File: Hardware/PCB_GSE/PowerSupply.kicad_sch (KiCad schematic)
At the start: 64 parts, among them J8 Vin_XT30PW-F, U1 L6981N33DR, U3 MPQ9843GLE-5-AEC1-Z, U7 LM2673SX-12_NOPB

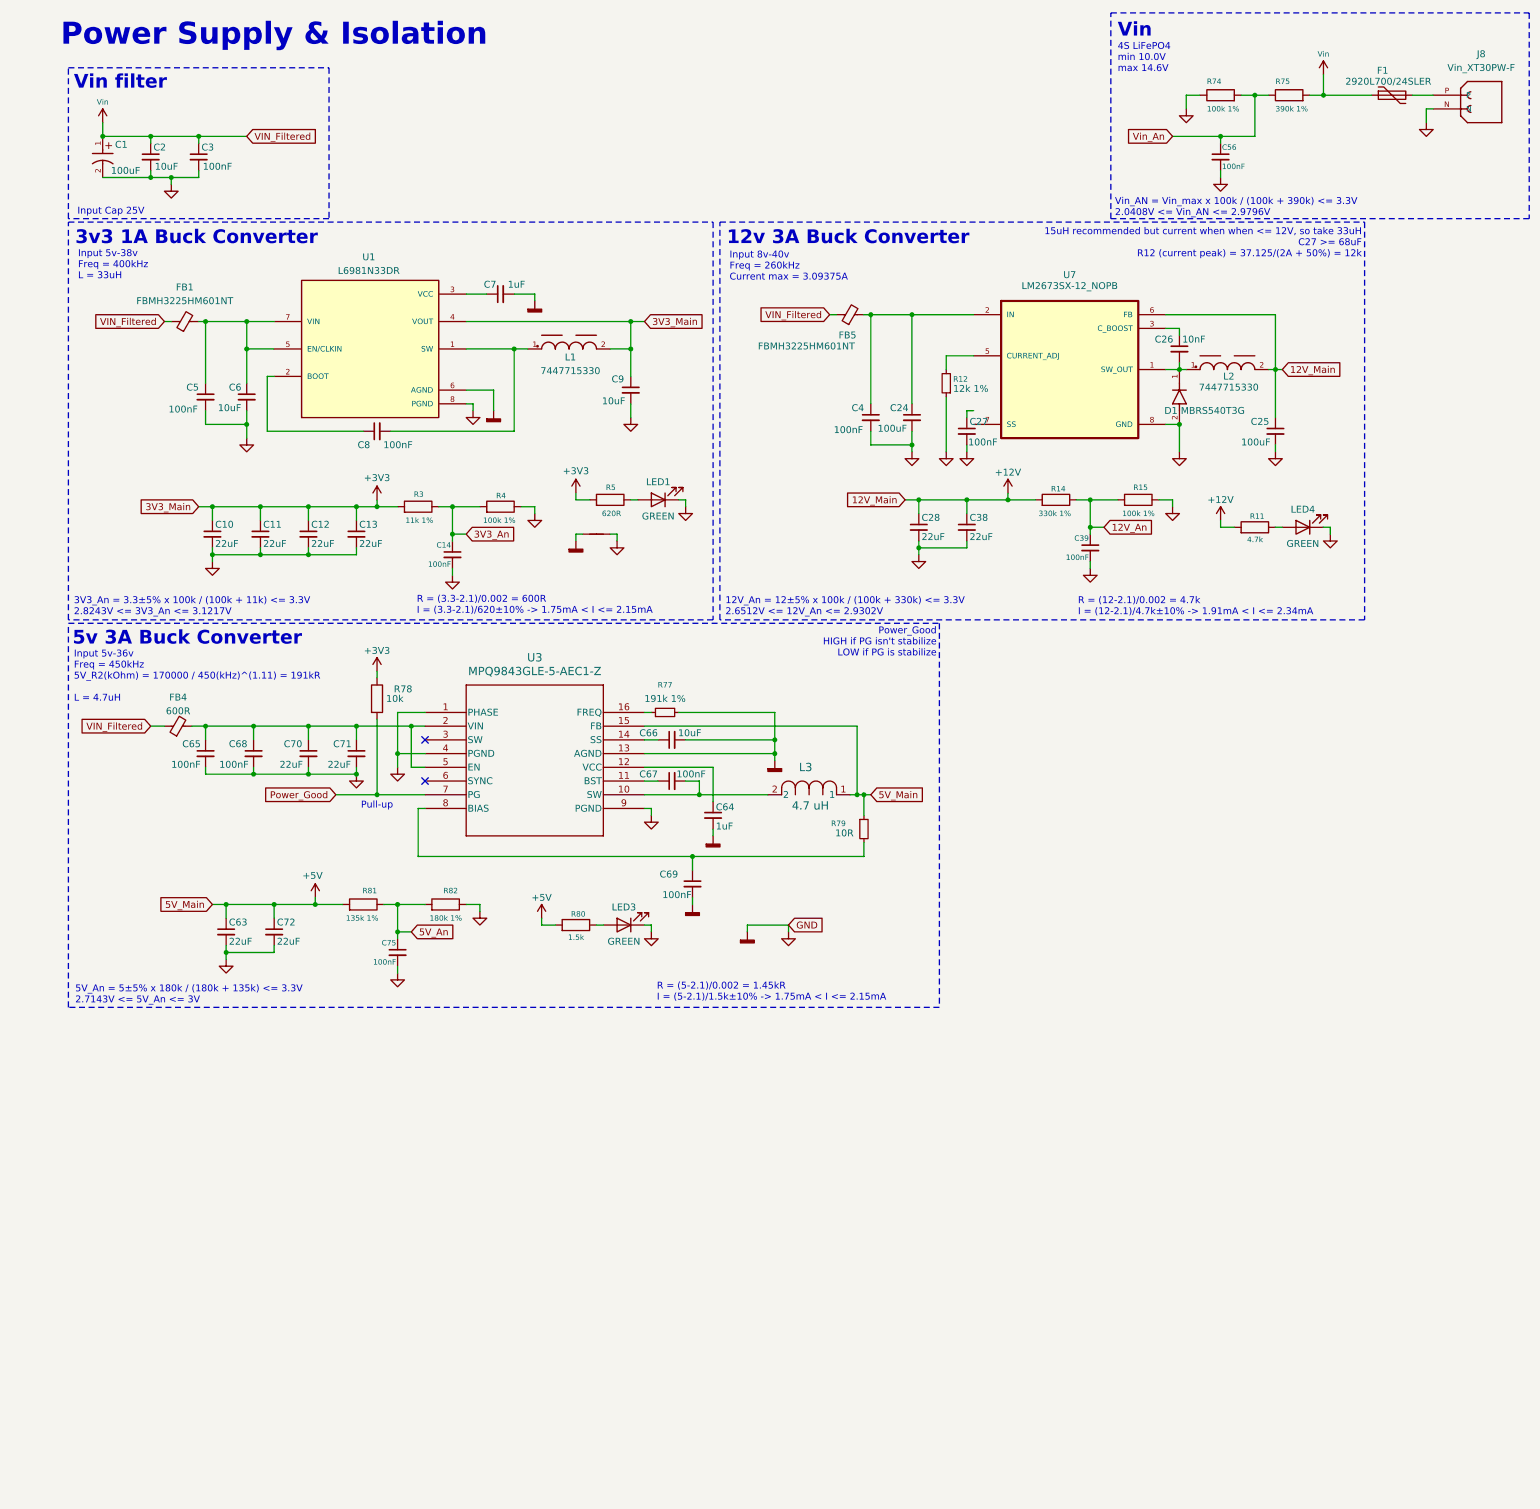
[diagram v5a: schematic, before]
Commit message: feat: change buck 3v3 1A ->5V 3A to 3.3V 1A cascade LDO + add symbol/footprint
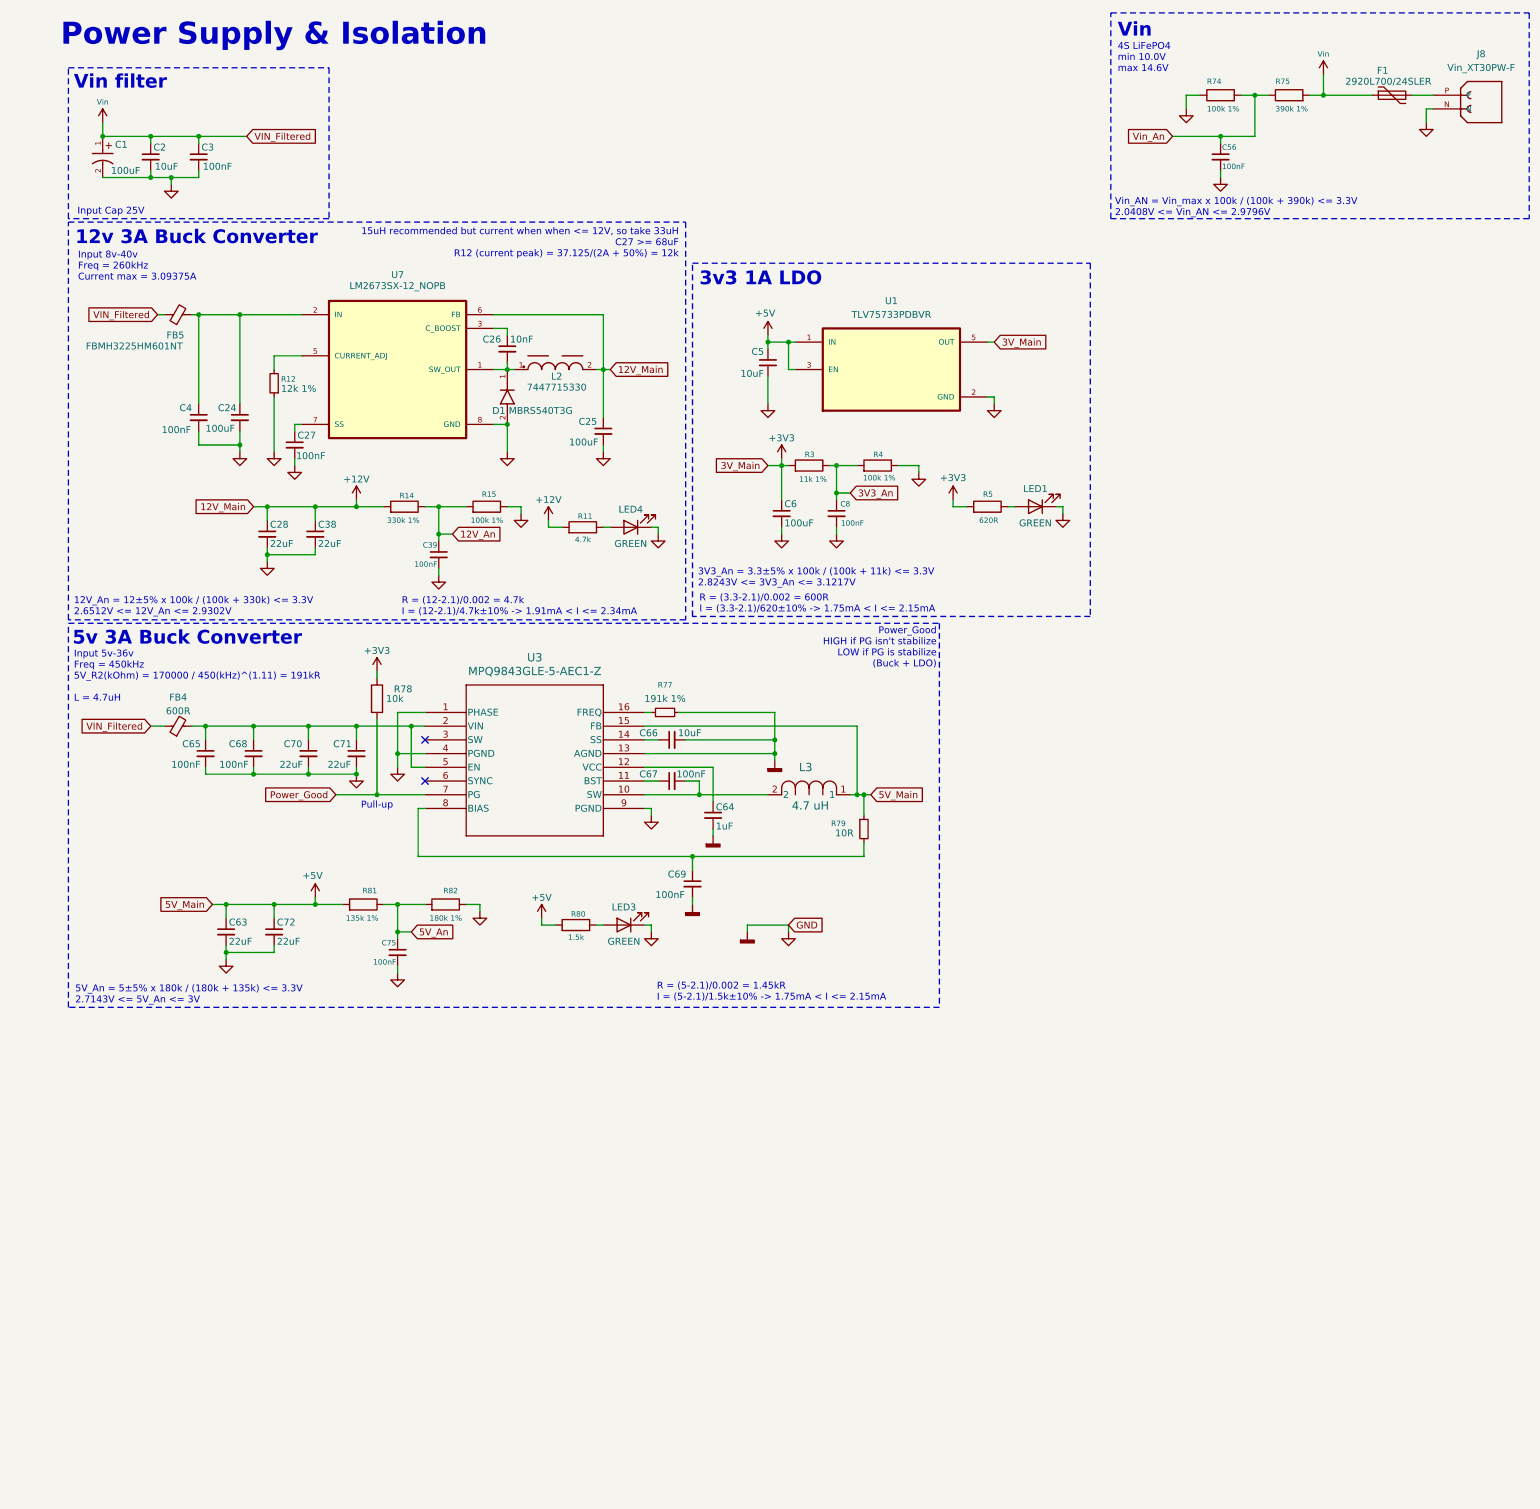
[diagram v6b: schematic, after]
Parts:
- removed C10, C11, C12, C13: 22uF, Capacitor_SMD:C_0805_2012Metric, symbol Device:C_Small
- removed C14: 100nF, Capacitor_SMD:C_0805_2012Metric, symbol Device:C_Small
- removed C7: 1uF, Capacitor_SMD:C_0805_2012Metric, symbol Device:C_Small
- removed C9: 10uF, Capacitor_SMD:C_0805_2012Metric, symbol Device:C_Small
- removed FB1: FBMH3225HM601NT, Inductor_SMD:L_1210_3225Metric, symbol Device:FerriteBead_Small
- removed L1: 7447715330, WE-PD_1245:WE-PD_1245, symbol PCB_GSE:WE-PD_1245
- removed NT4: NetTie_2, NetTie:NetTie-4_SMD_Pad0.5mm, symbol Device:NetTie_2
- removed U1: L6981N33DR, L6981N33DR:SOIC127P600X175-8N, symbol PCB_GSE:L6981N33DR
- added U1: TLV75733PDBVR, TLV75733PDBVR:SOT95P280X145-5N, symbol PCB_GSE:TLV75733PDBVR
- C5: value 100nF -> 10uF
- C6: value 10uF -> 100uF; DigiKey_Part_Number (none) -> 445-14428-1-ND; Manufacturer_Part_Number (none) -> C2012X5R1V226M125AC
- C8: footprint Capacitor_SMD:C_0805_2012Metric -> ODB:C_0402_1005Metric; DigiKey_Part_Number (none) -> 311-3342-1-ND; Manufacturer_Part_Number (none) -> CC0402KRX5R9BB104
- R3: footprint Resistor_SMD:R_0805_2012Metric -> Resistor_SMD:R_0603_1608Metric; DigiKey_Part_Number (none) -> 13-RT0603BRD07135KLCT-ND; Manufacturer_Part_Number (none) -> RT0603BRD07135KL
- R4: footprint Resistor_SMD:R_0805_2012Metric -> Resistor_SMD:R_0603_1608Metric; DigiKey_Part_Number (none) -> P180KDBCT-ND; Manufacturer_Part_Number (none) -> ERA-3AEB184V
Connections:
- net +3V3: now also C6.1, U1.5 (OUT)
- net +5V: now also C5.1, U1.1 (IN), U1.3 (EN)
- net 3V3_An: now also C8.1
- net AGND5V: now also C8.2, U1.2 (GND)
- net at C27.1: now also U7.7 (SS)
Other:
- note added: "3v3 1A LDO"
- note added: "Power_Good HIGH if PG isn't stabilize LOW if PG is stabilize (Buck + LDO)"
- note removed: "3v3 1A Buck Converter"
- note removed: "Input 5v-38v Freq = 400kHz L = 33uH"
- note removed: "Power_Good HIGH if PG isn't stabilize LOW if PG is stabilize"
- moved on the sheet: C24, C25, C26, C27, C28, C38, C39, C4, D1, FB5, L2, LED1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

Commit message: refactor: merge emile + main branches
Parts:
- renumbered C1 to C10, C2 to C11, C3 to C12, C4 to C13, C65 to C14, C63 to C15, C24 to C16, C68 to C17, C28 to C18, C72 to C19, C27 to C20, C70 to C21, C38 to C22, C71 to C23, C75 to C24, C39 to C25, C25 to C27, C66 to C28, C67 to C29, C69 to C30, C64 to C31, C5 to C32, C6 to C33, C8 to C34, C56 to C35, FB5 to FB2, FB4 to FB3, J8 to J2, L2 to L1, L3 to L2, LED3 to LED2, LED4 to LED3, LED1 to LED4, R12 to R10, R81 to R11, R78 to R12, R14 to R13, R82 to R14, R80 to R16, R11 to R17, R77 to R18, R3 to R19, R79 to R20, R4 to R21, R5 to R22, R74 to R23, R75 to R24, U7 to U2, U1 to U4
